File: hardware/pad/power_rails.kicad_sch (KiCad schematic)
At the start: 15 parts, among them U4 TPS2116DRL, U5 TPS61023DRLR

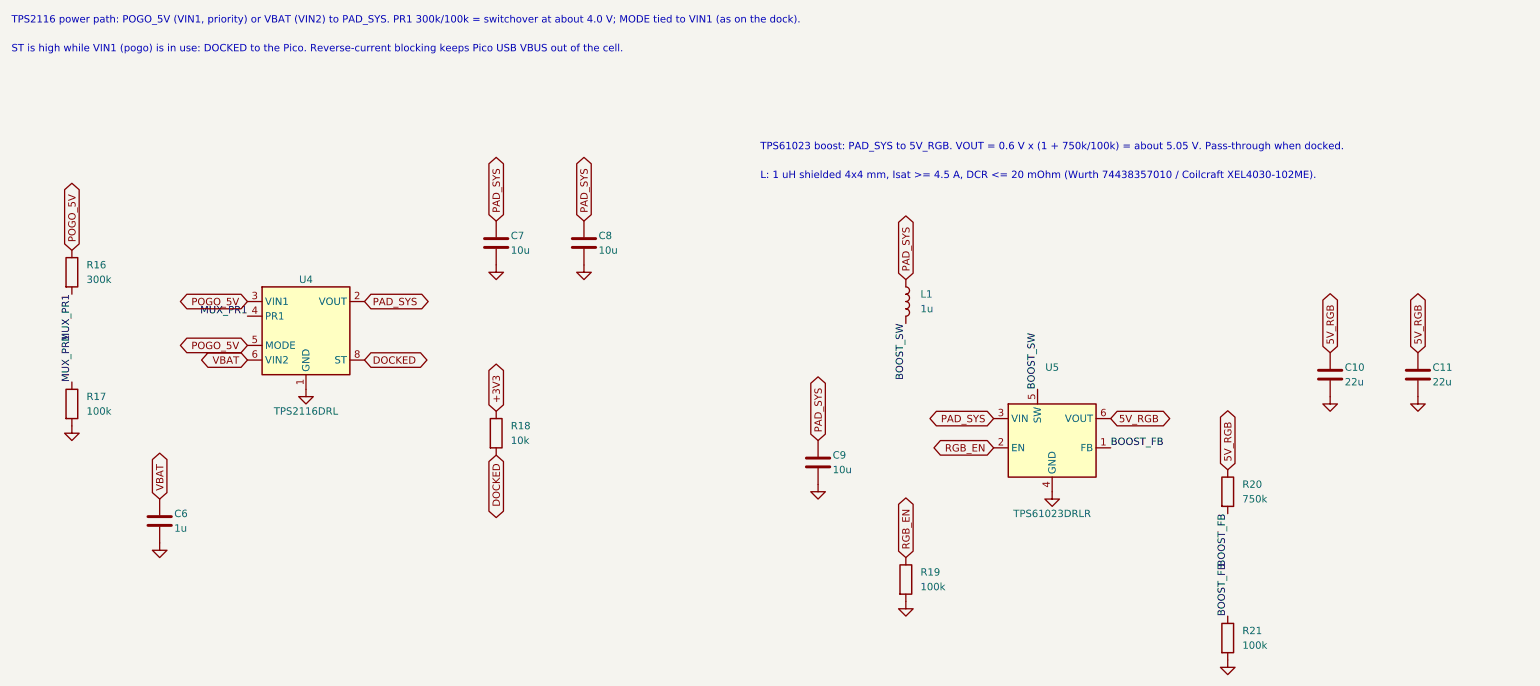
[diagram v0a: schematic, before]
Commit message: Pad schematic: hand-redrawn from the connection guide; netlist verified against the reference
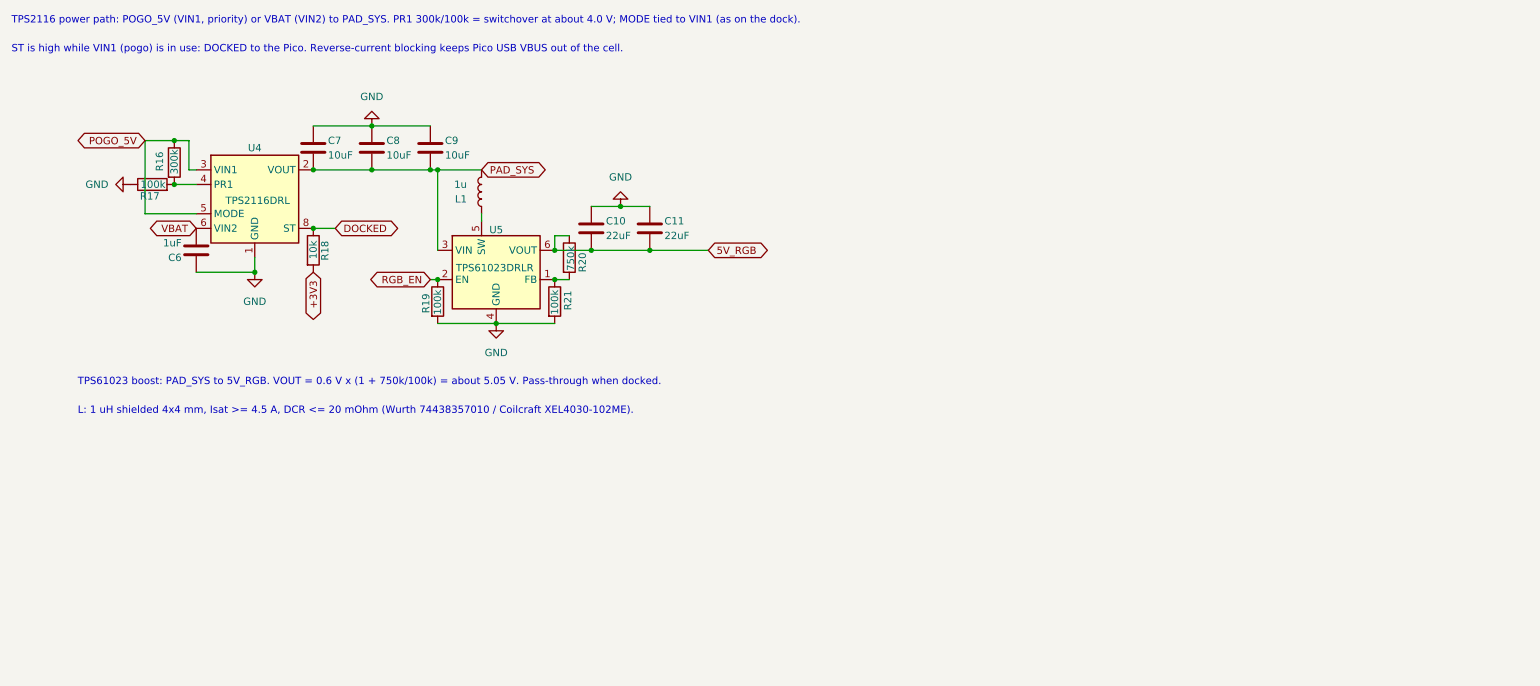
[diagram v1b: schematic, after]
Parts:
- C10, C11: value 22u -> 22uF
- C6: value 1u -> 1uF
- C7, C8, C9: value 10u -> 10uF
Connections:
- net +3V3: now also R18.2; no longer R18.1
- net 5V_RGB: now also C10.2, C11.2; no longer C10.1, C11.1
- net DOCKED: now also R18.1; no longer R18.2
- net GND: now also C10.1, C11.1, C6.1, C7.1, C8.1, C9.1, R17.1; no longer C10.2, C11.2, C6.2, C7.2, C8.2, C9.2, R17.2
- net PAD_SYS: now also C7.2, C8.2, C9.2, L1.2; no longer C7.1, C8.1, C9.1, L1.1
- net VBAT: now also C6.2; no longer C6.1
- net BOOST_FB: no longer names the net of R20.2, R21.1, U5.1 (FB)
- net BOOST_SW: no longer names the net of U5.5 (SW)
- net BOOST_SW: now also L1.1; no longer L1.2
- net MUX_PR1: no longer names the net of R16.2, U4.4 (PR1)
- net MUX_PR1: now also R17.2; no longer R17.1
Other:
- moved on the sheet: U4, U5
